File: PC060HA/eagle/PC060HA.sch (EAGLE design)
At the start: 13 parts, among them IC22 PC060HA, IC8 LM1117MPX-3.3

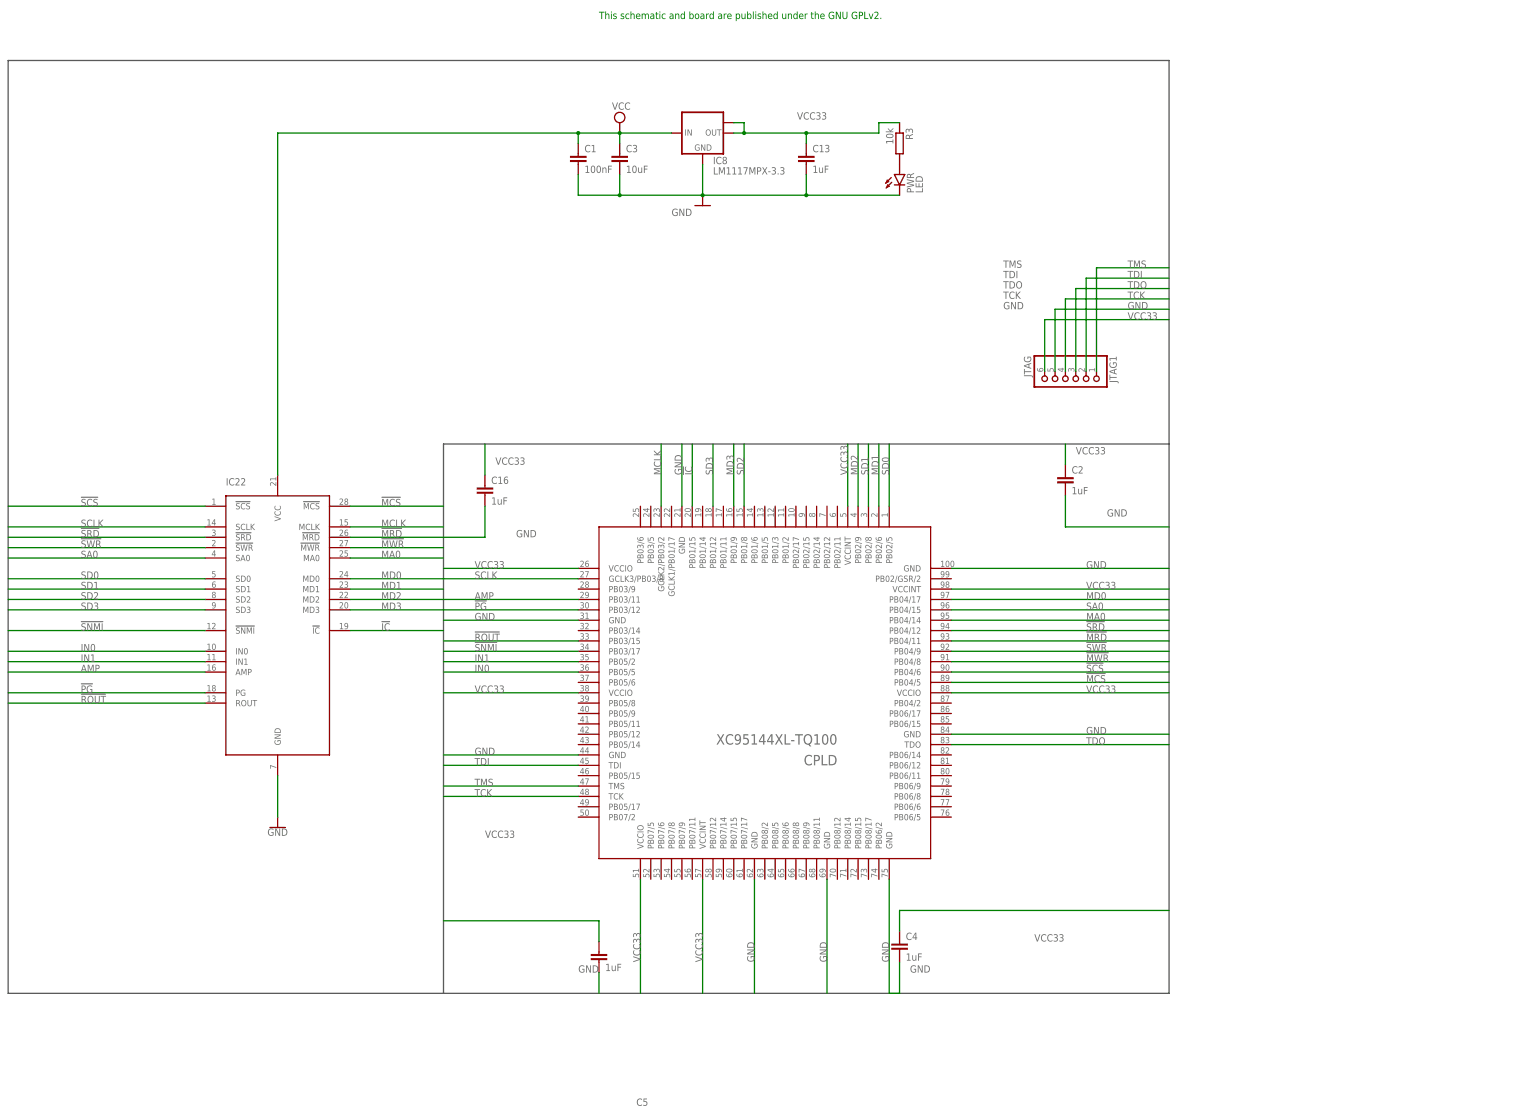
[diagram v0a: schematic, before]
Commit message: shrunk down to small board with SMD DiL
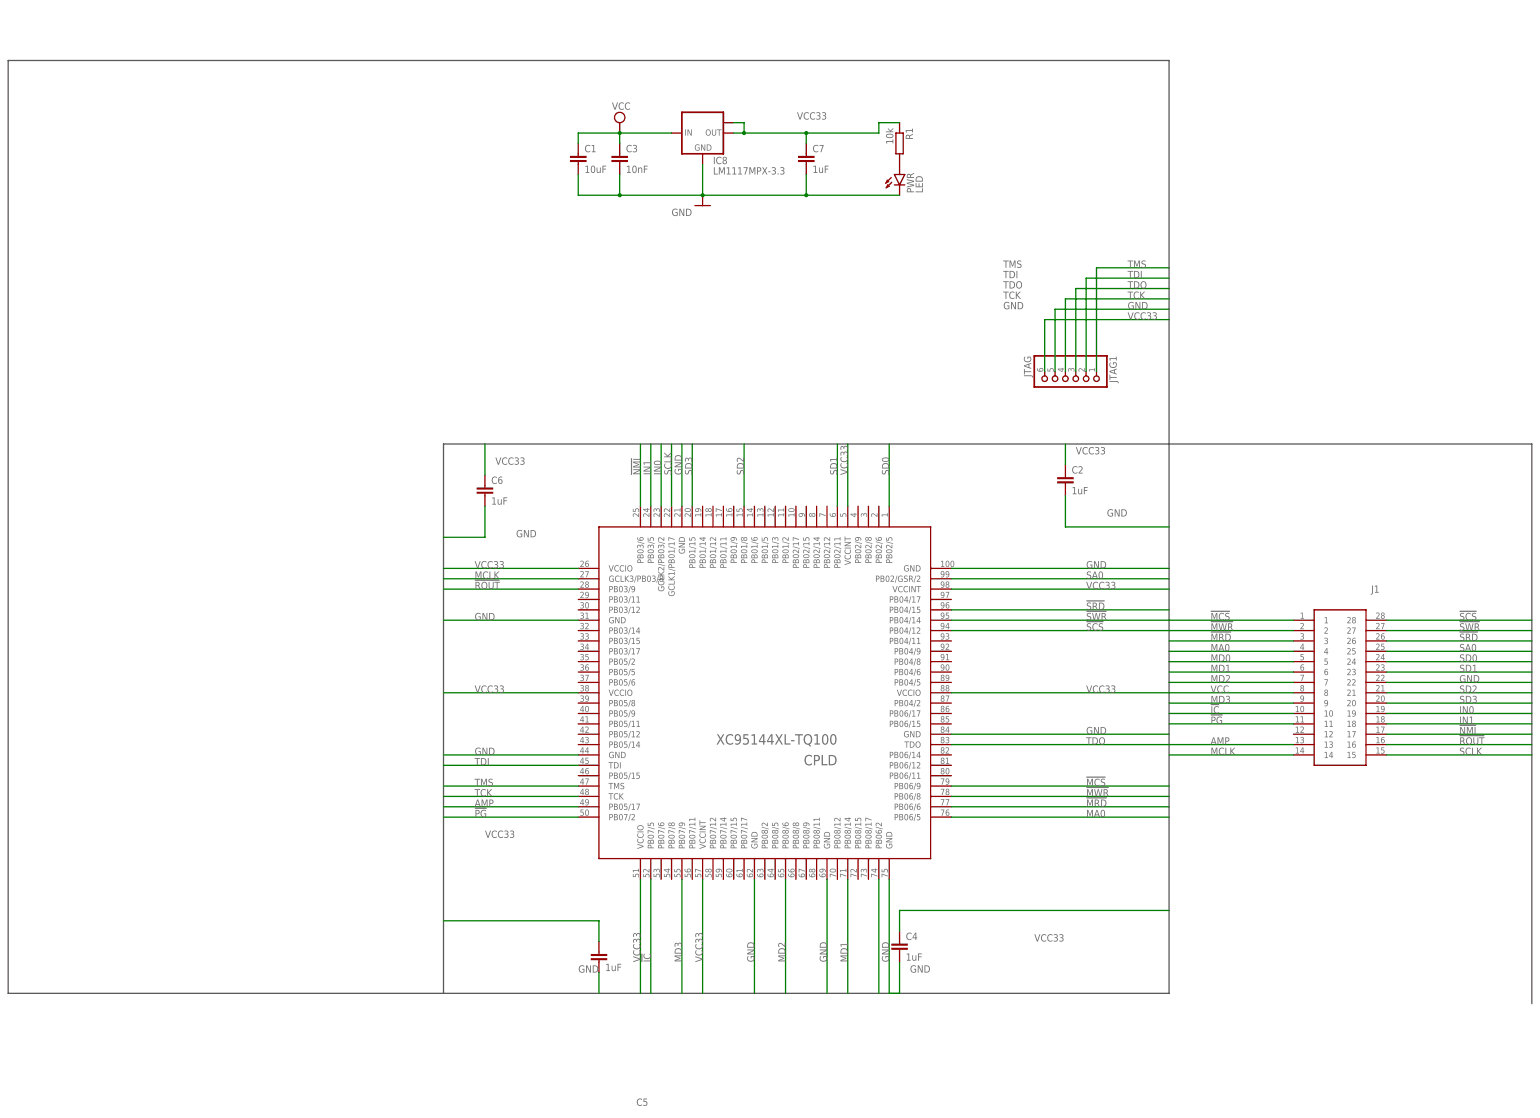
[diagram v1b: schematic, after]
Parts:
- removed IC22: PC060HA, OpWolf:PC060HA
- added J1: 150-10-628-00-106161, SamacSys_Parts:150-10-628-00-106161
- C1: value 100nF -> 10uF
- C3: value 10uF -> 10nF
- renumbered C13 to C7, C16 to C6, R3 to R1
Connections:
- removed net !SNMI: CPLD.PB03/17, IC22.!SNMI
- new net !NMI: CPLD.PB03/6, J1.17
- net !IC: now also CPLD.PB07/5, J1.10; no longer CPLD.PB01/15, IC22.!IC
- net !MCS: now also CPLD.PB06/9, J1.1; no longer CPLD.PB04/5, IC22.!MCS
- net !MRD: now also CPLD.PB06/6, J1.3; no longer CPLD.PB04/11, IC22.!MRD
- net !MWR: now also CPLD.PB06/8, J1.2; no longer CPLD.PB04/8, IC22.!MWR
- net !PG: now also CPLD.PB07/2, J1.11; no longer CPLD.PB03/12, IC22.PG
- net !ROUT: now also CPLD.PB03/9, J1.16; no longer CPLD.PB03/15, IC22.ROUT
- net !SCS: now also CPLD.PB04/12, J1.28; no longer CPLD.PB04/6, IC22.!SCS
- net !SRD: now also CPLD.PB04/15, J1.26; no longer CPLD.PB04/12, IC22.!SRD
- net !SWR: now also CPLD.PB04/14, J1.27; no longer CPLD.PB04/9, IC22.!SWR
- net AMP: now also CPLD.PB05/17, J1.13; no longer CPLD.PB03/11, IC22.AMP
- net GND: now also J1.22; no longer IC22.GND
- net IN0: now also CPLD.GCLK2/PB03/2, J1.19; no longer CPLD.PB05/5, IC22.IN0
- net IN1: now also CPLD.PB03/5, J1.18; no longer CPLD.PB05/2, IC22.IN1
- net MA0: now also CPLD.PB06/5, J1.4; no longer CPLD.PB04/14, IC22.MA0
- net MCLK: now also CPLD.GCLK3/PB03/8, J1.14; no longer CPLD.GCLK2/PB03/2, IC22.MCLK
- net MD0: now also CPLD.PB06/2, J1.5; no longer CPLD.PB04/17, IC22.MD0
- net MD1: now also CPLD.PB08/14, J1.6; no longer CPLD.PB02/6, IC22.MD1
- net MD2: now also CPLD.PB08/6, J1.7; no longer CPLD.PB02/9, IC22.MD2
- net MD3: now also CPLD.PB07/9, J1.9; no longer CPLD.PB01/9, IC22.MD3
- net SA0: now also CPLD.PB02/GSR/2, J1.25; no longer CPLD.PB04/15, IC22.SA0
- net SCLK: now also CPLD.GCLK1/PB01/17, J1.15; no longer CPLD.GCLK3/PB03/8, IC22.SCLK
- net SD0: now also J1.24; no longer IC22.SD0
- net SD1: now also CPLD.PB02/11, J1.23; no longer CPLD.PB02/8, IC22.SD1
- net SD2: now also J1.21; no longer IC22.SD2
- net SD3: now also CPLD.PB01/15, J1.20; no longer CPLD.PB01/12, IC22.SD3
- net VCC: now also J1.8; no longer IC22.VCC
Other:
- note removed: "This schematic and board are published under the GNU GPLv2."
